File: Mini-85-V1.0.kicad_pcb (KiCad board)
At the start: 2 copper layers, 56.3 x 41.6 mm, 38 parts, among them J2 AVR-ISP-6, J3 Screw_Terminal_01x08, J4 VIN, SW1 SW_Push, U1 ATtiny85-20S

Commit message: feat se vrea repo
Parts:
- removed the H4 at (172.2, 116.0)
- removed kibuzzard-65F8F6EE: G***, kibuzzard-65F8F6EE
- added D3: LEDRELE, LED_SMD:LED_1206_3216Metric_Pad1.42x1.75mm_HandSolder, F.Cu at (181.9, 80.5)
- added D4: 1N5400, Diode_THT:D_A-405_P7.62mm_Horizontal, F.Cu at (177.3, 81.0)
- added H1: MountingHole, MountingHole:MountingHole_3.2mm_M3_ISO14580_Pad_TopBottom, F.Cu at (71.1, 80.8)
- added H2: MountingHole, MountingHole:MountingHole_3.2mm_M3_ISO14580_Pad_TopBottom, F.Cu at (193.5, 118.6)
- added J1: Screw_Terminal_01x08, TerminalBlock_Phoenix:TerminalBlock_Phoenix_MKDS-3-8-5.08_1x08_P5.08mm_Horizontal, F.Cu at (130.3, 115.6)
- added J5: Screw_Terminal_01x04, TerminalBlock_Phoenix:TerminalBlock_Phoenix_MKDS-3-4-5.08_1x04_P5.08mm_Horizontal, F.Cu at (172.0, 115.6)
- added K1: G5LE-1, Relay_THT:Relay_SPDT_Omron-G5LE-1, F.Cu at (177.5, 88.1)
- added Q1: 2N7002H, Package_TO_SOT_SMD:SOT-23, F.Cu at (188.1, 87.6)
- added R4: 1k, Resistor_SMD:R_0805_2012Metric_Pad1.20x1.40mm_HandSolder, F.Cu at (181.6, 83.3)
- added R5: 10K, Resistor_SMD:R_0805_2012Metric_Pad1.20x1.40mm_HandSolder, F.Cu at (188.0, 92.5)
- added kibuzzard-65F8FC0E: G***, kibuzzard-65F8FC0E, F.Cu at (186.9, 109.0)
- added kibuzzard-66664CF2: G***, kibuzzard-66664CF2, F.Cu at (121.4, 109.0)
- added kibuzzard-66664DCB: G***, kibuzzard-66664DCB, F.Cu at (171.4, 109.0)
- added kibuzzard-66664E03: G***, kibuzzard-66664E03, F.Cu at (177.0, 109.0)
- added kibuzzard-66664E1D: G***, kibuzzard-66664E1D, F.Cu at (182.1, 109.0)
- J3: value Screw_Terminal_01x08 -> VIN; footprint TerminalBlock_Phoenix:TerminalBlock_Phoenix_MKDS-3-8-5.08_1x08_P5.08mm_Horizontal -> TerminalBlock_Phoenix:TerminalBlock_Phoenix_MKDS-3-2-5.08_1x02_P5.08mm_Horizontal
- J4: value VIN -> Conn_01x03_Female; footprint TerminalBlock_Phoenix:TerminalBlock_Phoenix_MKDS-3-2-5.08_1x02_P5.08mm_Horizontal -> Connector_PinHeader_2.54mm:PinHeader_1x03_P2.54mm_Vertical
- moved J4 61.8 mm to (188.2, 104.1), turned to 180 degrees
- moved H4 21.6 mm to (193.5, 82.0)
- moved G*** 21.3 mm to (193.4, 109.3)
- moved G*** 21.3 mm to (193.5, 102.2)
- moved G*** 21.3 mm to (193.3, 91.7)
- moved G*** 21.3 mm to (193.4, 98.8)
- moved G*** 21.3 mm to (193.5, 105.7)
- moved G*** 21.3 mm to (193.3, 88.2)
- moved G*** 21.3 mm to (193.4, 95.2)
- moved J3 11.5 mm to (127.8, 100.8), turned to 90 degrees
- moved kibuzzard-65F8FC0E 10.3 mm to (160.8, 108.5)
- moved kibuzzard-65F8FC7A 10.2 mm to (155.7, 108.5)
- moved kibuzzard-65F8FCA8 10.2 mm to (150.9, 108.5)
- moved kibuzzard-65F8FD72 10.2 mm to (145.5, 108.5)
- moved kibuzzard-65F903CA 10.1 mm to (130.3, 108.5)
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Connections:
- J3 pad 1: +5V -> GND
- J3 pad 2: /MOSI -> +12V
- J4 pad 1: GND -> unconnected-(J4-Pin_1-Pad1)
- J4 pad 2: +12V -> Net-(J4-Pin_2)
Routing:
- net +12V: track 104.2 -> 150.6 mm
- net Net-(J4-Pin_2): track 0.00 -> 45.9 mm
- net +5V: track 81.5 -> 120.5 mm, vias 1 -> 2
- net Net-(D4-A): track 0.00 -> 30.3 mm
- net Net-(J5-Pin_3): track 0.00 -> 13.9 mm
- net Net-(J5-Pin_1): track 0.00 -> 13.4 mm
- net /PB4: track 48.6 -> 40.7 mm, vias 0 -> 2
- net /SCK: track 31.3 -> 35.0 mm
- net /PB3: track 51.2 -> 54.8 mm
- net /MOSI: track 43.3 -> 47.0 mm
- net /MISO: track 29.3 -> 32.7 mm
- net Net-(D3-A): track 0.00 -> 3.14 mm
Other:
- board size 56.3 x 41.6 mm -> 78.6 x 44.2 mm

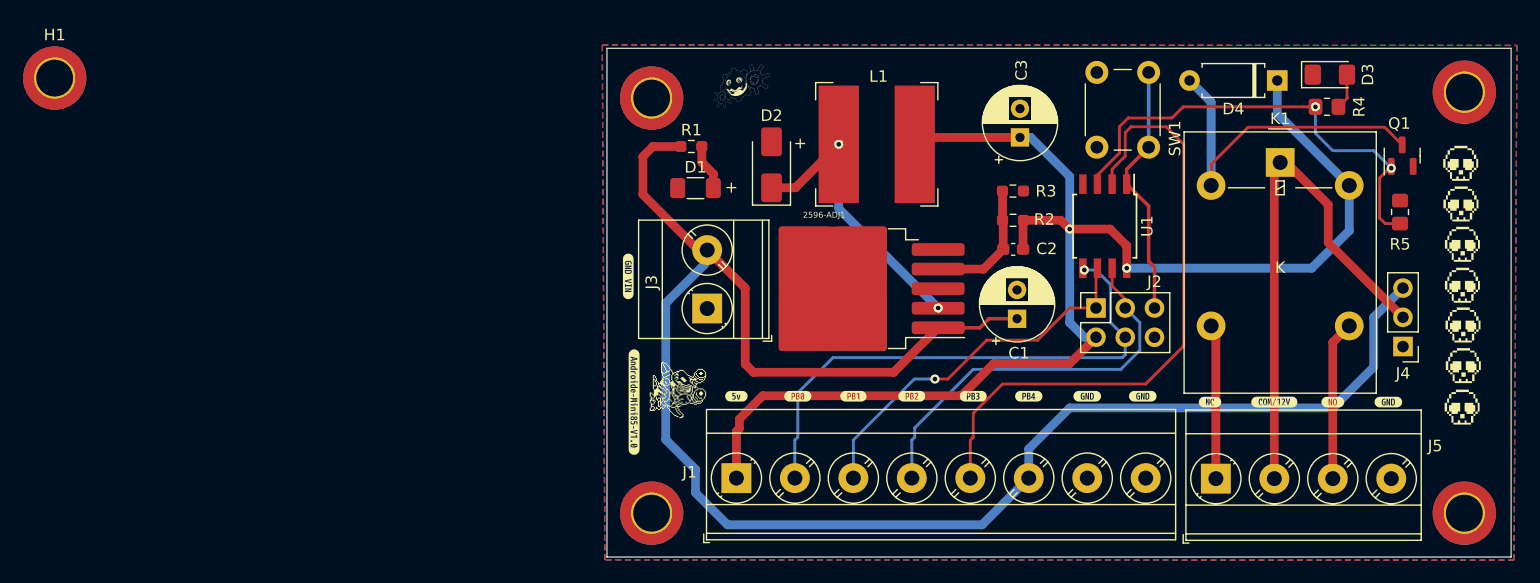
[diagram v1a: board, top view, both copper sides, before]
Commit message: feat: ajuste de placa
agujeros de sijecion de placa aplicados
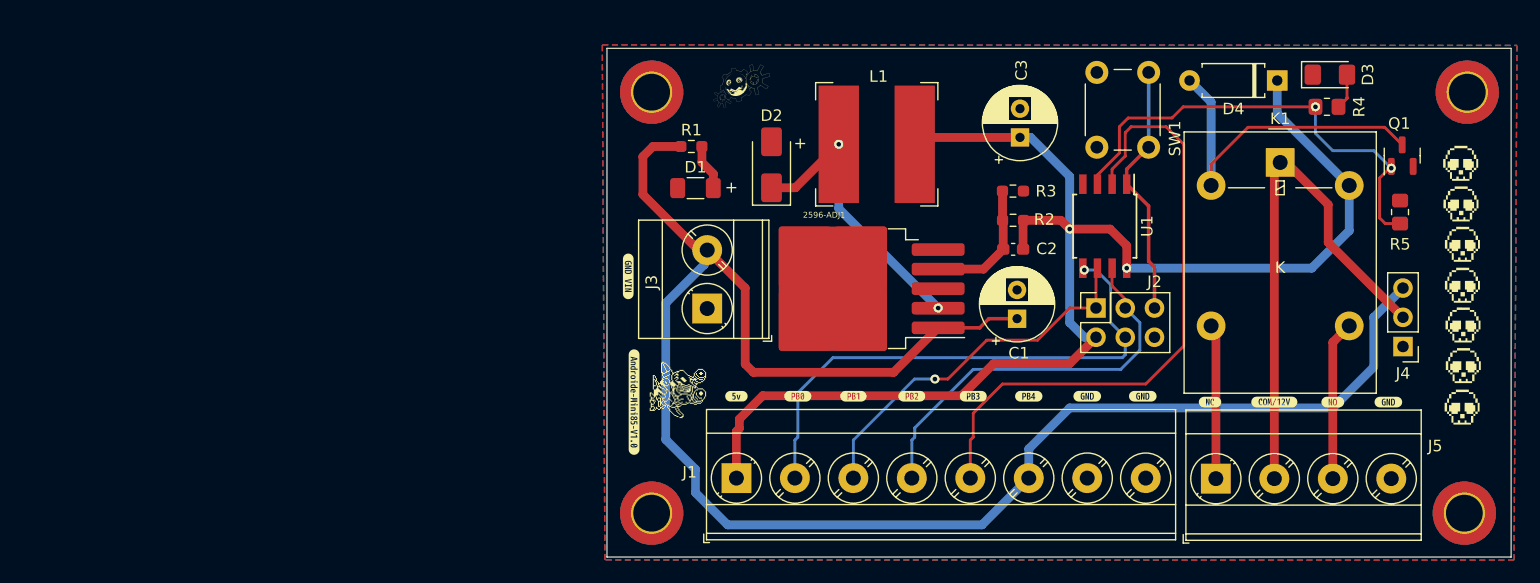
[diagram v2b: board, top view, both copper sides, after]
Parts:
- removed H1: MountingHole, MountingHole:MountingHole_3.2mm_M3_ISO14580_Pad_TopBottom
- moved H4 0.51 mm to (122.9, 82.0)
- moved H4 0.25 mm to (193.8, 82.0)
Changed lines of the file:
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@@
     (fp_line (start 1 0.625) (end -1 0.625)
       (stroke (width 0.1) (type solid)) (layer "F.Fab"))
-    (pad "1" smd roundrect (at -1 0) (size 1.2 1.4) (layers "F.Cu" "F.Paste" "F.Mask") (roundrect_rratio 0.208333)
+    (pad "1" smd roundrect (at -1 0) (size 1.2 1.4) (layers "F.Cu" "F.Paste" "F.Mask") (roundrect_rratio 0.2083333333)
       (net 9 "/PB4") (pintype "passive"))
-    (pad "2" smd roundrect (at 1 0) (size 1.2 1.4) (layers "F.Cu" "F.Paste" "F.Mask") (roundrect_rratio 0.208333)
+    (pad "2" smd roundrect (at 1 0) (size 1.2 1.4) (layers "F.Cu" "F.Paste" "F.Mask") (roundrect_rratio 0.2083333333)
       (net 13 "Net-(D3-A)") (pintype "passive"))
     (model "${KICAD6_3DMODEL_DIR}/Resistor_SMD.3dshapes/R_0805_2012Metric.wrl"
@@
     (fp_line (start 1 0.625) (end -1 0.625)
       (stroke (width 0.1) (type solid)) (layer "F.Fab"))
-    (pad "1" smd roundrect (at -1 0 90) (size 1.2 1.4) (layers "F.Cu" "F.Paste" "F.Mask") (roundrect_rratio 0.208333)
+    (pad "1" smd roundrect (at -1 0 90) (size 1.2 1.4) (layers "F.Cu" "F.Paste" "F.Mask") (roundrect_rratio 0.2083333333)
       (net 9 "/PB4") (pintype "passive"))
-    (pad "2" smd roundrect (at 1 0 90) (size 1.2 1.4) (layers "F.Cu" "F.Paste" "F.Mask") (roundrect_rratio 0.208333)
+    (pad "2" smd roundrect (at 1 0 90) (size 1.2 1.4) (layers "F.Cu" "F.Paste" "F.Mask") (roundrect_rratio 0.2083333333)
       (net 3 "GND") (pintype "passive"))
     (model "${KICAD6_3DMODEL_DIR}/Resistor_SMD.3dshapes/R_0805_2012Metric.wrl"
@@
     (attr board_only exclude_from_pos_files exclude_from_bom)
     (fp_text reference "kibuzzard-66664E03" (at 0 -3.522927) (layer "F.SilkS") hide
-        (effects (font (size 0 0)))
+        (effects (font (size 0 0) (thickness 0.15)))
     )
     (fp_text value "G***" (at 0 3.522927) (layer "F.SilkS") hide
-        (effects (font (size 0 0)))
+        (effects (font (size 0 0) (thickness 0.15)))
     )
     (fp_poly
@@
     (attr board_only exclude_from_pos_files exclude_from_bom)
     (fp_text reference "kibuzzard-66664E1D" (at 0 -3.511021) (layer "F.SilkS") hide
-        (effects (font (size 0 0)))
+        (effects (font (size 0 0) (thickness 0.15)))
     )
     (fp_text value "G***" (at 0 3.511021) (layer "F.SilkS") hide
-        (effects (font (size 0 0)))
+        (effects (font (size 0 0) (thickness 0.15)))
     )
     (fp_poly
@@
     (fp_line (start 1.6 0.8) (end 1.6 -0.8)
       (stroke (width 0.1) (type solid)) (layer "F.Fab"))
-    (pad "1" smd roundrect (at -1.4875 0) (size 1.425 1.75) (layers "F.Cu" "F.Paste" "F.Mask") (roundrect_rratio 0.175439)
+    (pad "1" smd roundrect (at -1.4875 0) (size 1.425 1.75) (layers "F.Cu" "F.Paste" "F.Mask") (roundrect_rratio 0.1754392982)
       (net 3 "GND") (pinfunction "K") (pintype "passive"))
-    (pad "2" smd roundrect (at 1.4875 0) (size 1.425 1.75) (layers "F.Cu" "F.Paste" "F.Mask") (roundrect_rratio 0.175439)
+    (pad "2" smd roundrect (at 1.4875 0) (size 1.425 1.75) (layers "F.Cu" "F.Paste" "F.Mask") (roundrect_rratio 0.1754392982)
       (net 13 "Net-(D3-A)") (pinfunction "A") (pintype "passive"))
     (model "${KICAD6_3DMODEL_DIR}/LED_SMD.3dshapes/LED_1206_3216Metric.wrl"
@@
     )
   )
-  (footprint "MountingHole:MountingHole_3.2mm_M3_ISO14580_Pad_TopBottom" (layer "F.Cu")
-    (at 71.0685 80.816)
-    (descr "Mounting Hole 3.2mm, M3, ISO14580")
-    (tags "mounting hole 3.2mm m3 iso14580")
-    (property "Sheetfile" "Barra de luz.kicad_sch")
-    (property "Sheetname" "")
-    (property "ki_description" "Mounting Hole without connection")
-    (property "ki_keywords" "mounting hole")
-    (attr exclude_from_pos_files)
-    (fp_text reference "H1" (at 0 -3.75) (layer "F.SilkS")
-        (effects (font (size 1 1) (thickness 0.15)))
-    )
-    (fp_text value "MountingHole" (at 0 3.75) (layer "F.Fab")
-        (effects (font (size 1 1) (thickness 0.15)))
-    )
-    (fp_text user "${REFERENCE}" (at 0 0) (layer "F.Fab")
-        (effects (font (size 1 1) (thickness 0.15)))
-    )
-    (fp_circle (center 0 0) (end 2.75 0)
-      (stroke (width 0.15) (type solid)) (fill none) (layer "Cmts.User"))
-    (fp_circle (center 0 0) (end 3 0)
-      (stroke (width 0.05) (type solid)) (fill none) (layer "F.CrtYd"))
-    (pad "1" thru_hole circle (at 0 0) (size 3.6 3.6) (drill 3.2) (layers "*.Cu" "*.Mask"))
-    (pad "1" connect circle (at 0 0) (size 5.5 5.5) (layers "F.Cu" "F.Mask"))
-    (pad "1" connect circle (at 0 0) (size 5.5 5.5) (layers "B.Cu" "B.Mask"))
-  )
   (footprint "LOGO" (layer "F.Cu")
     (at 193.294 91.694)
@@
   )
   (footprint "MountingHole:MountingHole_3.2mm_M3_ISO14580_Pad_TopBottom" (layer "F.Cu")
-    (at 122.936 82.55 180)
+    (at 122.936 82.042 180)
     (descr "Mounting Hole 3.2mm, M3, ISO14580")
     (tags "mounting hole 3.2mm m3 iso14580")
@@
   )
   (footprint "MountingHole:MountingHole_3.2mm_M3_ISO14580_Pad_TopBottom" (layer "F.Cu")
-    (at 193.548 82.042 180)
+    (at 193.802 82.042 180)
     (descr "Mounting Hole 3.2mm, M3, ISO14580")
     (tags "mounting hole 3.2mm m3 iso14580")
@@
     (attr board_only exclude_from_pos_files exclude_from_bom)
     (fp_text reference "kibuzzard-66664CF2" (at 0 -3.518958 -90) (layer "F.SilkS") hide
-        (effects (font (size 0 0)))
+        (effects (font (size 0 0) (thickness 0.15)))
     )
     (fp_text value "G***" (at 0 3.518958 -90) (layer "F.SilkS") hide
-        (effects (font (size 0 0)))
+        (effects (font (size 0 0) (thickness 0.15)))
     )
     (fp_poly
@@
     (attr board_only exclude_from_pos_files exclude_from_bom)
     (fp_text reference "kibuzzard-66664DCB" (at 0 -3.511021) (layer "F.SilkS") hide
-        (effects (font (size 0 0)))
+        (effects (font (size 0 0) (thickness 0.15)))
     )
     (fp_text value "G***" (at 0 3.511021) (layer "F.SilkS") hide
-        (effects (font (size 0 0)))
+        (effects (font (size 0 0) (thickness 0.15)))
     )
     (fp_poly
